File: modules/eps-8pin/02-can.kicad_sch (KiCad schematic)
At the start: 6 parts, among them U2 TJA1051T/3

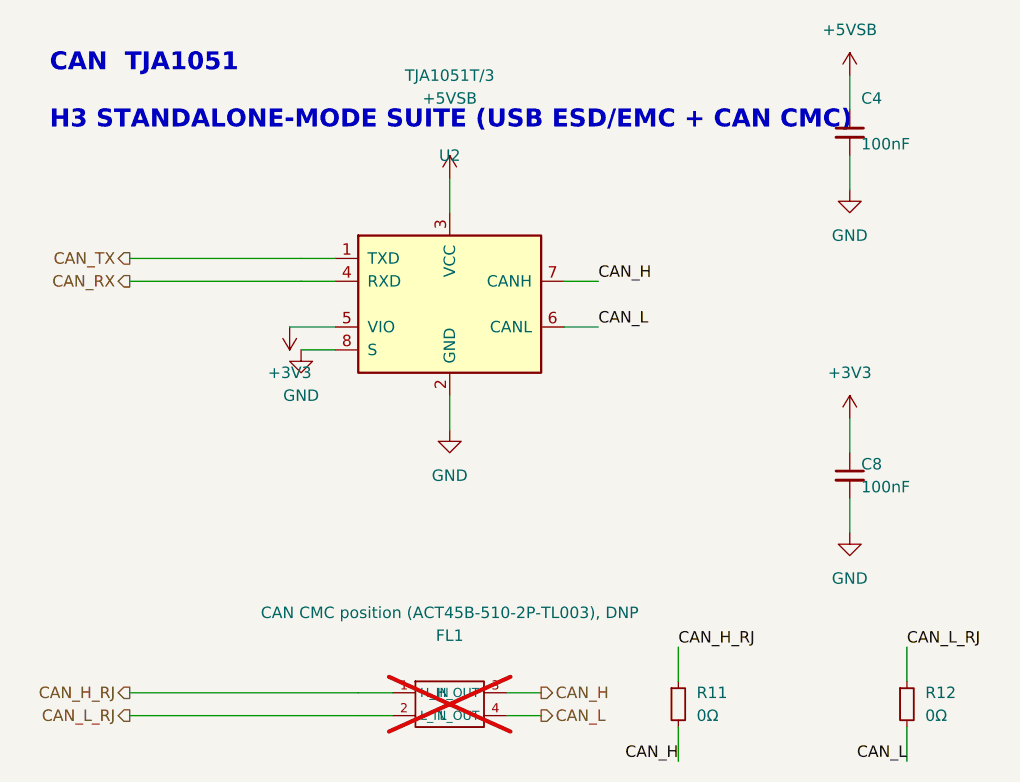
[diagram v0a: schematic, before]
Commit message: Looking through boards and figuring out outlines.
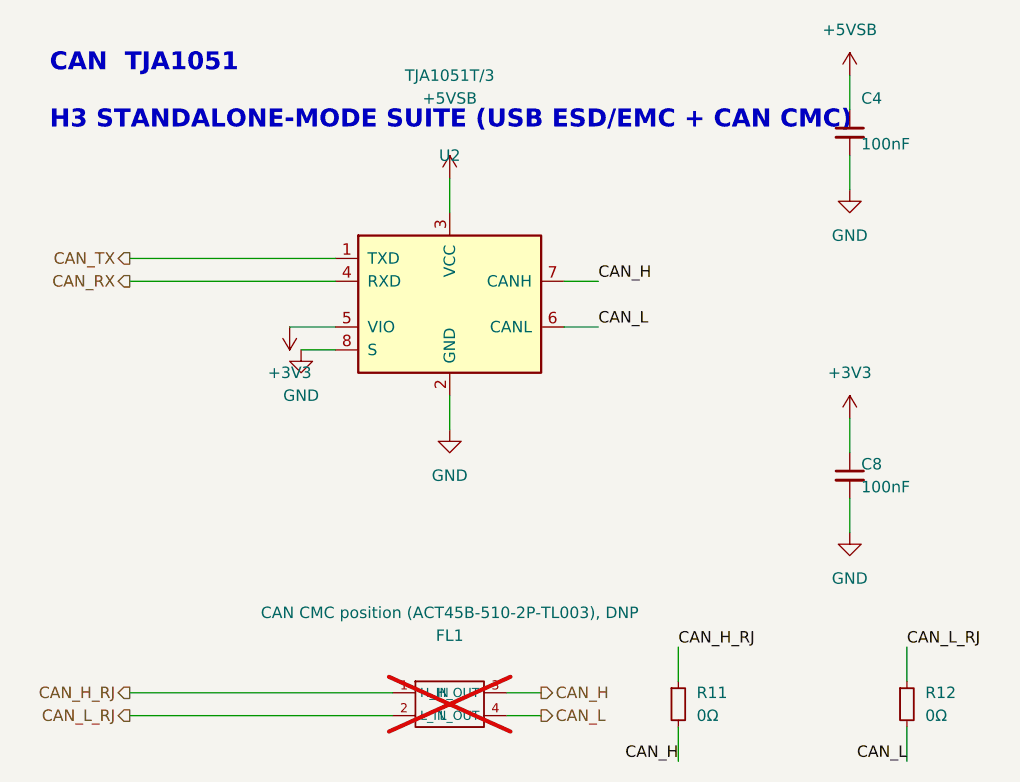
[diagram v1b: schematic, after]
